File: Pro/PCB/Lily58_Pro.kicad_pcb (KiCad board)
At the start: 2 copper layers, 142.5 x 106.3 mm, 87 parts, among them J1 LED, J2 4PIN, J3 OLED, P1 i2c_pin, P2 i2c_pin, SW1 SW_PUSH, SW10 SW_PUSH, SW11 SW_PUSH, SW12 SW_PUSH, SW13 SW_PUSH, SW14 SW_PUSH, SW15 SW_PUSH, SW16 SW_PUSH, SW17 SW_PUSH, SW18 SW_PUSH, SW19 SW_PUSH, SW2 SW_PUSH, SW20 SW_PUSH, SW21 SW_PUSH, SW22 SW_PUSH, SW23 SW_PUSH, SW24 SW_PUSH, SW25 SW_PUSH, SW26 SW_PUSH, SW27 SW_PUSH, SW28 SW_PUSH, SW29 SW_PUSH, SW3 SW_PUSH, SW4 SW_PUSH, SW5 SW_PUSH, SW6 SW_PUSH, SW7 SW_PUSH, SW8 SW_PUSH, SW9 SW_PUSH, U1 ProMicro

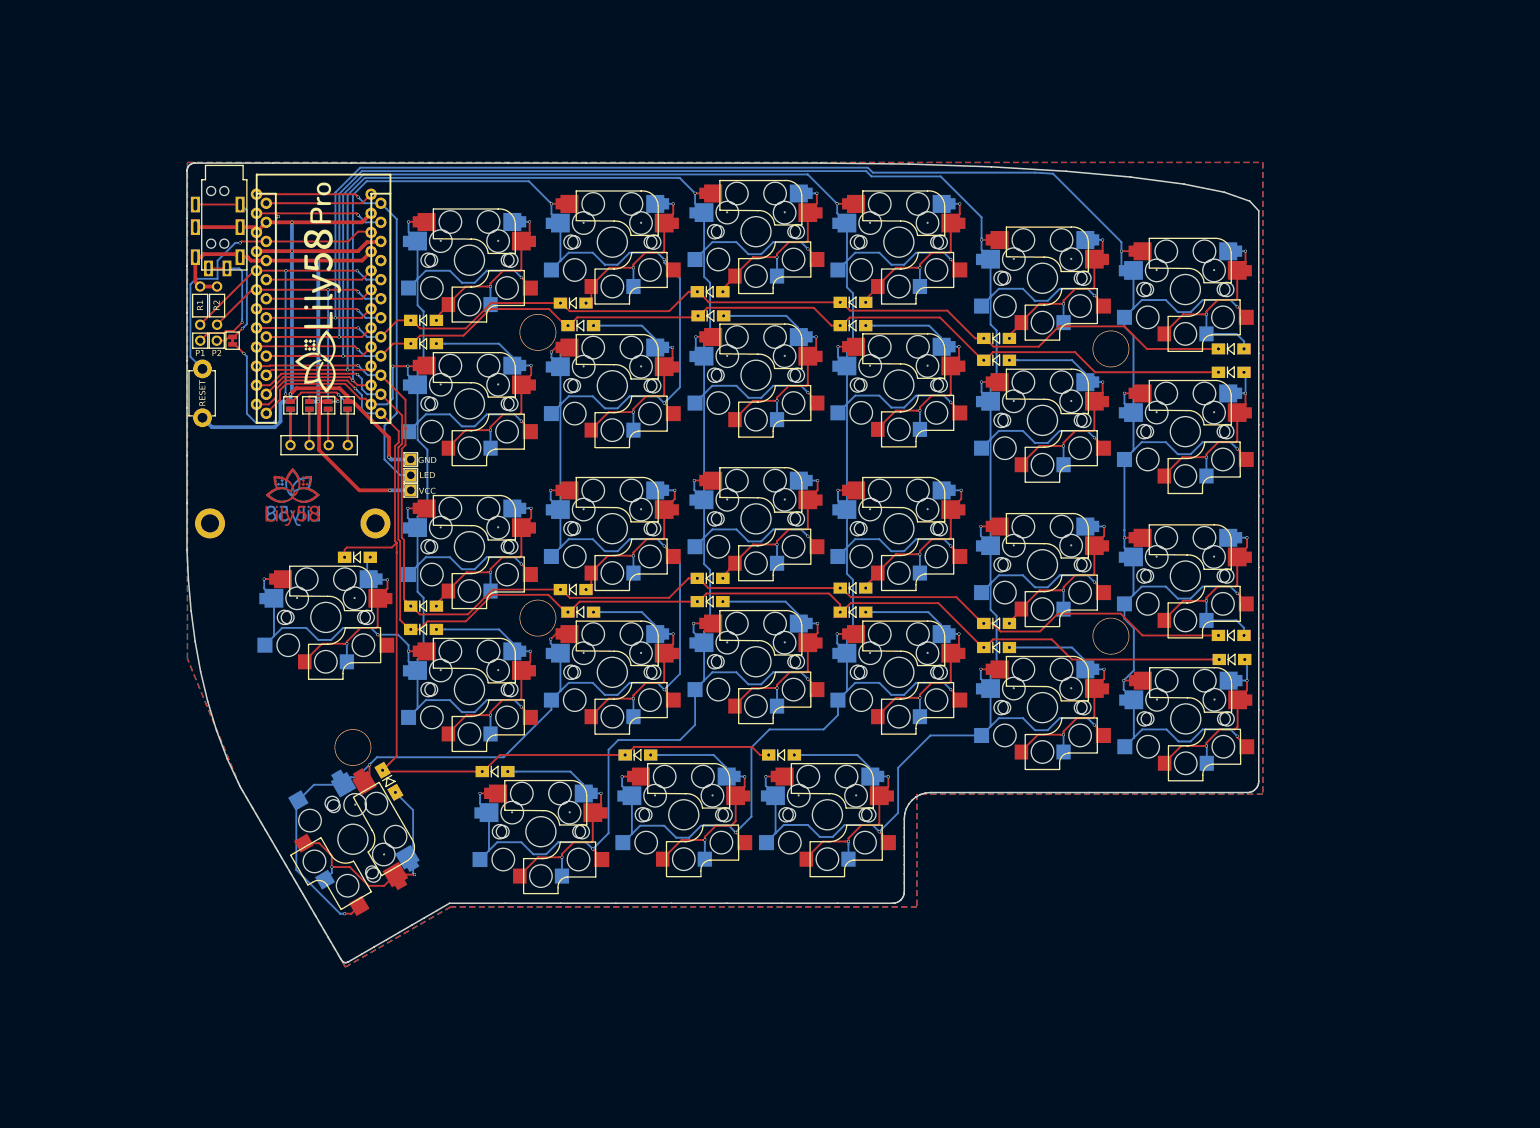
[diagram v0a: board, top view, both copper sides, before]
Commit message: Adjust thumb positions, add battery switch
Also powers/charges both sides
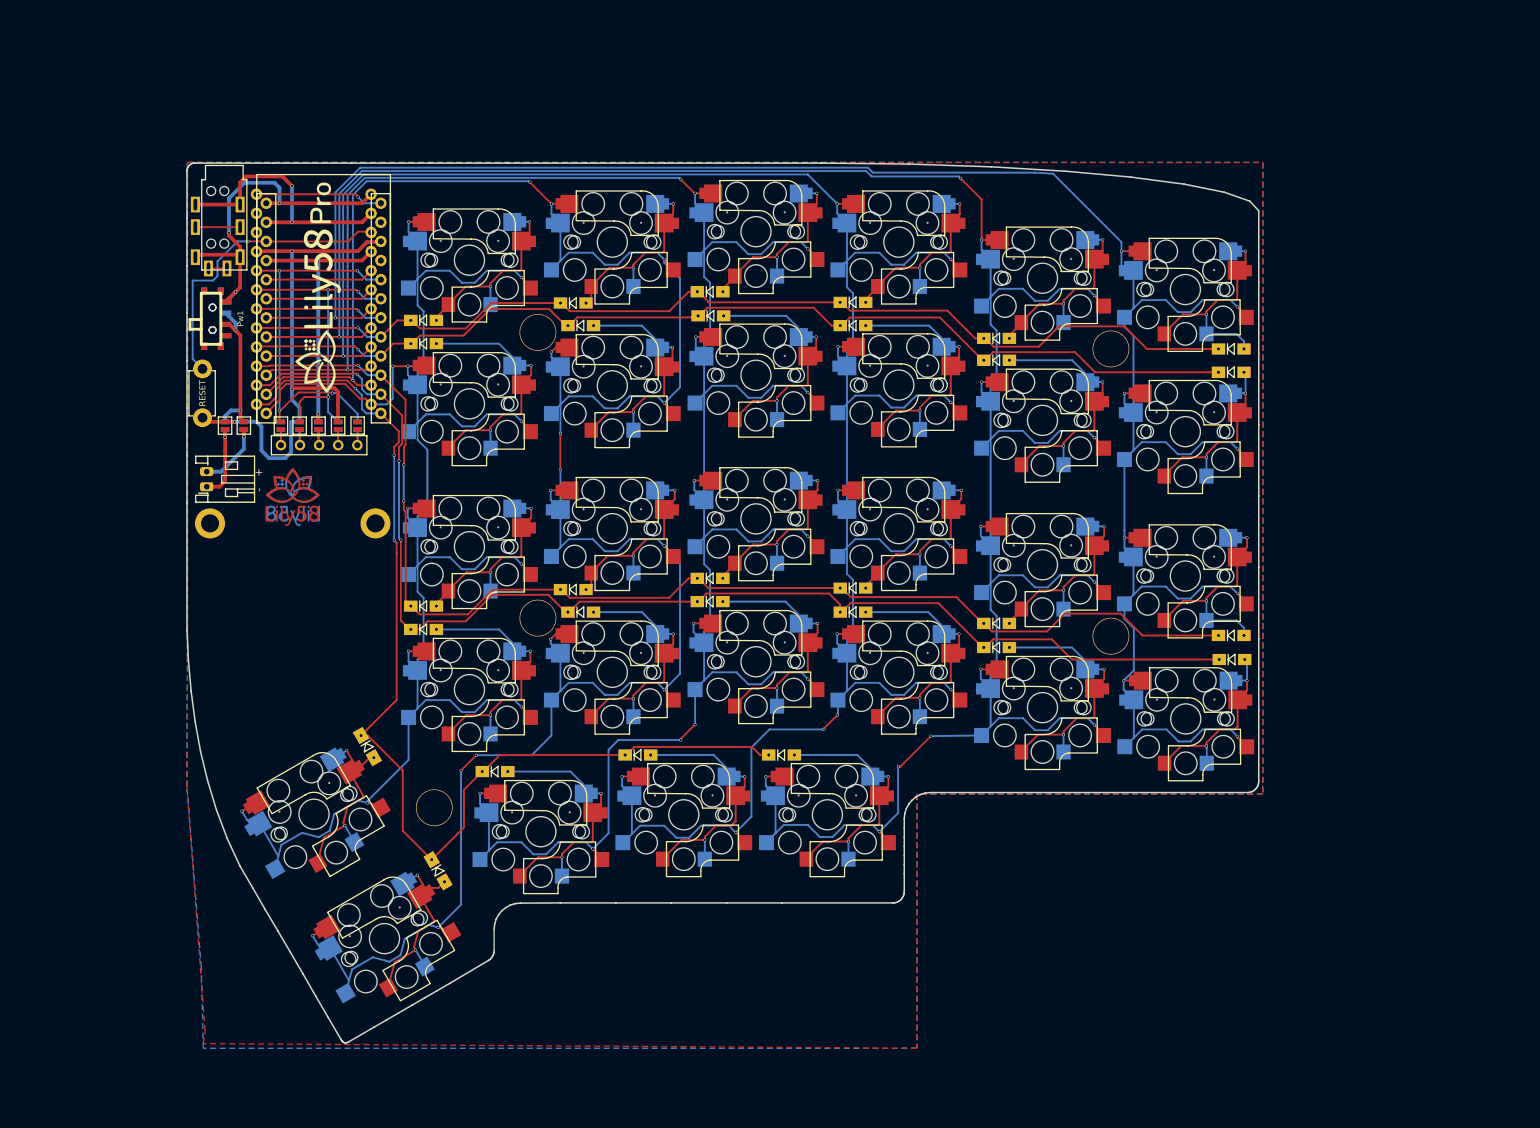
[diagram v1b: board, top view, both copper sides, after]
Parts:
- removed the J1 at (112.7, 81.1)
- removed P1, P2: i2c_pin, Lily58-footprint:1pin_conn
- removed R1, R2: R, Lily58-footprint:RESISTOR_mini
- removed W1: jumper, Lily58-footprint:jumper_data
- added BT1: Battery_Cell, Connector_JST:JST_PH_S2B-PH-K_1x02_P2.00mm_Horizontal, F.Cu at (85.6, 80.1)
- added JP1: Jumper_NO_Small, Lily58-footprint:Jumper, F.Cu at (105.6, 72.0)
- added JP11: Device:Jumper_NO_Small, Lily58-footprint:Jumper, F.Cu at (90.5, 72.0)
- added JP12: Device:Jumper_NO_Small, Lily58-footprint:Jumper, F.Cu at (88.0, 72.0)
- added JP13: Device:Jumper_NO_Small, Lily58-footprint:Jumper, B.Cu at (90.5, 72.0)
- added JP14: Device:Jumper_NO_Small, Lily58-footprint:Jumper, B.Cu at (88.0, 72.0)
- added JP6: JP6, Lily58-footprint:Jumper, B.Cu at (105.6, 72.0)
- added Pw1: SW_SPDT, open-project:SWITCH_ALPS_SSSS8, F.Cu at (84.8, 57.8)
- added Pw2: SW_SPDT, open-project:SWITCH_ALPS_SSSS8, B.Cu at (84.8, 57.8)
- JP10: renamed from JP8; value (none) -> Jumper_NO_Small
- JP2: renamed from JP1; value (none) -> Jumper_NO_Small
- JP3: renamed from JP2; value (none) -> Jumper_NO_Small
- JP4: renamed from JP3; value (none) -> Jumper_NO_Small
- JP5: renamed from JP4; value (none) -> Jumper_NO_Small
- JP7: renamed from JP5; value (none) -> Jumper_NO_Small
- JP8: renamed from JP6; value (none) -> Jumper_NO_Small
- JP9: renamed from JP7; value (none) -> Jumper_NO_Small
- SW1: footprint Lily58-footprint:CherryMX_KailhLowProfile_Hotswap_edge -> Lily58-footprint:MX_Choc_Hotswap
- SW10: renamed from SW26; footprint Lily58-footprint:CherryMX_KailhLowProfile_Hotswap_edge -> Lily58-footprint:MX_Choc_Hotswap
- SW11: renamed from SW3; footprint Lily58-footprint:CherryMX_KailhLowProfile_Hotswap_edge -> Lily58-footprint:MX_Choc_Hotswap
- SW12: renamed from SW9; footprint Lily58-footprint:CherryMX_KailhLowProfile_Hotswap_edge -> Lily58-footprint:MX_Choc_Hotswap
- SW13: renamed from SW15; footprint Lily58-footprint:CherryMX_KailhLowProfile_Hotswap_edge -> Lily58-footprint:MX_Choc_Hotswap
- SW14: renamed from SW21; footprint Lily58-footprint:CherryMX_KailhLowProfile_Hotswap_edge -> Lily58-footprint:MX_Choc_Hotswap
- SW15: renamed from SW27; footprint Lily58-footprint:CherryMX_KailhLowProfile_Hotswap_edge -> Lily58-footprint:MX_Choc_Hotswap
- SW16: renamed from SW4; footprint Lily58-footprint:CherryMX_KailhLowProfile_Hotswap_edge -> Lily58-footprint:MX_Choc_Hotswap
- SW17: renamed from SW10; footprint Lily58-footprint:CherryMX_KailhLowProfile_Hotswap_edge -> Lily58-footprint:MX_Choc_Hotswap
- SW18: renamed from SW16; footprint Lily58-footprint:CherryMX_KailhLowProfile_Hotswap_edge -> Lily58-footprint:MX_Choc_Hotswap
- SW19: renamed from SW22; footprint Lily58-footprint:CherryMX_KailhLowProfile_Hotswap_edge -> Lily58-footprint:MX_Choc_Hotswap
- SW2: renamed from SW7; footprint Lily58-footprint:CherryMX_KailhLowProfile_Hotswap_edge -> Lily58-footprint:MX_Choc_Hotswap
- SW20: renamed from SW28; footprint Lily58-footprint:CherryMX_KailhLowProfile_Hotswap_edge -> Lily58-footprint:MX_Choc_Hotswap
- SW21: renamed from SW5; footprint Lily58-footprint:CherryMX_KailhLowProfile_Hotswap_edge -> Lily58-footprint:MX_Choc_Hotswap
- SW22: renamed from SW11; footprint Lily58-footprint:CherryMX_KailhLowProfile_Hotswap_edge -> Lily58-footprint:MX_Choc_Hotswap
- SW23: renamed from SW17; footprint Lily58-footprint:CherryMX_KailhLowProfile_Hotswap_edge -> Lily58-footprint:MX_Choc_Hotswap
- SW24: renamed from SW23; footprint Lily58-footprint:CherryMX_KailhLowProfile_Hotswap_edge -> Lily58-footprint:MX_Choc_Hotswap
- SW25: renamed from SW29; footprint Lily58-footprint:CherryMX_KailhLowProfile_Hotswap_edge -> Lily58-footprint:MX_Choc_Hotswap
- SW26: renamed from SW6; footprint Lily58-footprint:CherryMX_KailhLowProfile_Hotswap_edge -> Lily58-footprint:MX_Choc_Hotswap
- SW27: renamed from SW12; footprint Lily58-footprint:CherryMX_KailhLowProfile_Hotswap_edge -> Lily58-footprint:MX_Choc_Hotswap
- SW28: renamed from SW18; footprint Lily58-footprint:CherryMX_KailhLowProfile_Hotswap_edge -> Lily58-footprint:MX_Choc_Hotswap
- SW29: renamed from SW24; footprint Lily58-footprint:CherryMX_KailhLowProfile_Hotswap_edge -> Lily58-footprint:MX_Choc_Hotswap
- SW3: renamed from SW13; footprint Lily58-footprint:CherryMX_KailhLowProfile_Hotswap_edge -> Lily58-footprint:MX_Choc_Hotswap
- SW4: renamed from SW19; footprint Lily58-footprint:CherryMX_KailhLowProfile_Hotswap_edge -> Lily58-footprint:MX_Choc_Hotswap
- SW5: renamed from SW25; footprint Lily58-footprint:CherryMX_KailhLowProfile_Hotswap_edge -> Lily58-footprint:MX_Choc_Hotswap
- SW6: renamed from SW2; footprint Lily58-footprint:CherryMX_KailhLowProfile_Hotswap_edge -> Lily58-footprint:MX_Choc_Hotswap
- SW7: renamed from SW8; footprint Lily58-footprint:CherryMX_KailhLowProfile_Hotswap_edge -> Lily58-footprint:MX_Choc_Hotswap
- SW8: renamed from SW14; footprint Lily58-footprint:CherryMX_KailhLowProfile_Hotswap_edge -> Lily58-footprint:MX_Choc_Hotswap
- SW9: renamed from SW20; footprint Lily58-footprint:CherryMX_KailhLowProfile_Hotswap_edge -> Lily58-footprint:MX_Choc_Hotswap
- U1: value ProMicro -> NiceNano
- moved SW5 26.2 mm to (99.8, 123.7), turned to 30 degrees
- moved D5 25.2 mm to (106.9, 114.7), turned to -60 degrees
- moved SW10 13.9 mm to (109.2, 140.2), turned to 30 degrees
- moved D10 13.6 mm to (116.3, 131.2)
- moved TH7 13.5 mm to (115.8, 122.8)
- moved JP4 2.99 mm to (97.9, 72.0)
- moved JP2 2.99 mm to (103.0, 72.0)
- moved JP3 2.99 mm to (100.4, 72.0)
- moved JP10 2.98 mm to (95.4, 72.0)
- moved JP5 2.98 mm to (95.4, 72.0)
- moved JP7 2.98 mm to (103.0, 72.0)
- moved JP8 2.98 mm to (100.4, 72.0)
- moved JP9 2.98 mm to (97.9, 72.0)
- moved J1 1.27 mm to (95.4, 74.6)
- renumbered D26 to D10, D3 to D11, D9 to D12, D15 to D13, D21 to D14, D27 to D15, D4 to D16, D10 to D17, D16 to D18, D22 to D19, D7 to D2, D28 to D20, D5 to D21, D11 to D22, D17 to D23, D23 to D24, D29 to D25, D6 to D26, D12 to D27, D18 to D28, D24 to D29, D13 to D3, D19 to D4, D25 to D5, D2 to D6, D8 to D7, D14 to D8, D20 to D9, J3 to J1
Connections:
- J2 pad 1: VCC -> POWER
- J2 pad 2: GND -> unconnected-(J2-Pad2)
- J2 pad 3: Net-(J2-Pad3) -> GND
- J2 pad 4: Net-(J2-Pad4) -> unconnected-(J2-Pad4)
- JP10 pad 2: GND -> CS
- JP7 pad 2: SDA -> SCL
- JP8 pad 2: SCL -> VCC
- JP9 pad 2: VCC -> GND
- U1 pad 1: LED -> CS
- U1 pad 19: Net-(U1-Pad19) -> unconnected-(U1-A2(PF5)-Pad19)
- U1 pad 2: DATA -> unconnected-(U1-RX(PD2)-Pad2)
- U1 pad 20: Net-(U1-Pad20) -> unconnected-(U1-A3(PF4)-Pad20)
- U1 pad 24: Net-(U1-Pad24) -> POWER
- U1 pad 7: Net-(U1-Pad7) -> unconnected-(U1-D4(PD4)-Pad7)
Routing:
- net DATA: track 59.7 -> 0.00 mm, vias 3 -> 0
- net LED: track 57.0 -> 0.00 mm, vias 1 -> 0
- net POWER: track 0.00 -> 46.7 mm, vias 0 -> 3
- net VCC: track 72.9 -> 36.9 mm, vias 3 -> 2
- net Net-(J2-Pad3): track 26.6 -> 0.00 mm, vias 1 -> 0
- net BAT_POS: track 0.00 -> 20.2 mm, vias 0 -> 2
- net Net-(J2-Pad4): track 17.9 -> 0.00 mm, vias 1 -> 0
- net unconnected-(U1-D4(PD4)-Pad7): track 0.00 -> 17.0 mm, vias 0 -> 1
- net Net-(U1-Pad7): track 17.0 -> 0.00 mm, vias 1 -> 0
- net CS: track 0.00 -> 17.0 mm, vias 0 -> 1
- net unconnected-(U1-A3(PF4)-Pad20): track 0.00 -> 14.4 mm
- net unconnected-(U1-A2(PF5)-Pad19): track 0.00 -> 14.4 mm
- net Net-(U1-Pad24): track 14.4 -> 0.00 mm
- net Net-(U1-Pad20): track 14.4 -> 0.00 mm
- net Net-(U1-Pad19): track 14.4 -> 0.00 mm
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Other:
- board size 142.5 x 106.3 mm -> 142.5 x 117 mm
- net class Default removed
- net class GND removed
- net class VCC removed

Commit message: v1
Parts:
- G*** (x2): footprint Lily58-footprint:lily58_logo_Pro -> Lily58-footprint:iri58_logo_Pro
- G*** (x2): footprint Lily58-footprint:lily58_logo_2 -> Lily58-footprint:iris58_logo_2
- moved TH7 25.4 mm to (94.8, 108.5)
- moved SW10 4.71 mm to (110.4, 135.7)
- moved SW5 4.60 mm to (100.9, 119.2)
- moved D10 4.30 mm to (117.1, 127.0)
- moved D5 4.24 mm to (107.7, 110.5)
- moved G*** 3.51 mm to (100.5, 81.5) (x2)
- moved G*** 1.62 mm to (100.4, 55.2)
- moved G*** 1.62 mm to (100.4, 55.3)
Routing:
- net row4: track 142.6 -> 137.3 mm, vias 3 -> 4
- net col4: track 321.7 -> 316.8 mm
- net col5: track 242.6 -> 238.3 mm, vias 11 -> 10
- net Net-(D5-A): track 27.7 -> 26.9 mm
- net Net-(D10-A): track 27.6 -> 26.9 mm
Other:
- board size 142.5 x 117 mm -> 142.5 x 112.3 mm

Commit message: v2
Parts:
- removed D10, D11, D12, D13, D14, D15, D16, D17, D18, D19, D2, D20, D21, D22, D23, D24, D25, D26, D27, D28, D29, D3, D4, D5, D6, D7, D8, D9: D, Lily58-footprint:Diode_SOD123
- removed the G*** at (100.4, 55.2)
- removed the G*** at (100.4, 55.3)
- removed the JP3 at (100.4, 72.0)
- removed the JP8 at (100.4, 72.0)
- removed U1: NiceNano, Lily58-footprint:ProMicro_rev2
- added ENC1: RotaryEncoder_Switch, Rotary_Encoder:RotaryEncoder_Alps_EC11E-Switch_Vertical_H20mm, F.Cu at (88.8, 93.3)
- added JP13: ~, Lily58-footprint:Jumper_arrow, F.Cu at (90.6, 87.5)
- added JP14: ~, Lily58-footprint:Jumper_arrow, F.Cu at (93.1, 87.5)
- added JP15: ~, Lily58-footprint:Jumper_arrow, B.Cu at (90.6, 87.5)
- added JP16: ~, Lily58-footprint:Jumper_arrow, B.Cu at (93.1, 87.5)
- added MCU1: NiceNano, Lily58-footprint:ProMicro_rev3, F.Cu at (100.7, 51.2)
- D1: value D -> Lily58-cache:D
- J1: footprint Lily58-footprint:OLED_4Pin -> Lily58-footprint:NiceView_5Pin
- J2: value 4PIN -> TRRS
- JP1, JP2: value Jumper_NO_Small -> ~; footprint Lily58-footprint:Jumper -> Lily58-footprint:Jumper_arrow
- JP10: renamed from JP12; value Device:Jumper_NO_Small -> ~; footprint Lily58-footprint:Jumper -> Lily58-footprint:Jumper_arrow
- JP11: renamed from JP13; value Device:Jumper_NO_Small -> ~; footprint Lily58-footprint:Jumper -> Lily58-footprint:Jumper_arrow
- JP12: renamed from JP14; value Device:Jumper_NO_Small -> ~; footprint Lily58-footprint:Jumper -> Lily58-footprint:Jumper_arrow
- JP3: renamed from JP4; value Jumper_NO_Small -> ~; footprint Lily58-footprint:Jumper -> Lily58-footprint:Jumper_arrow
- JP4: renamed from JP5; value Jumper_NO_Small -> ~; footprint Lily58-footprint:Jumper -> Lily58-footprint:Jumper_arrow
- JP5: renamed from JP6; value JP6 -> ~; footprint Lily58-footprint:Jumper -> Lily58-footprint:Jumper_arrow
- JP6: renamed from JP7; value Jumper_NO_Small -> ~; footprint Lily58-footprint:Jumper -> Lily58-footprint:Jumper_arrow
- JP7: renamed from JP9; value Jumper_NO_Small -> ~; footprint Lily58-footprint:Jumper -> Lily58-footprint:Jumper_arrow
- JP8: renamed from JP10; value Jumper_NO_Small -> ~; footprint Lily58-footprint:Jumper -> Lily58-footprint:Jumper_arrow
- JP9: renamed from JP11; value Device:Jumper_NO_Small -> ~; footprint Lily58-footprint:Jumper -> Lily58-footprint:Jumper_arrow
- SW1: footprint Lily58-footprint:MX_Choc_Hotswap -> Lily58-footprint:MX_Choc_Hotswap_bottom_diode
- SW10: renamed from SW17; footprint Lily58-footprint:MX_Choc_Hotswap -> Lily58-footprint:MX_Choc_Hotswap_bottom_diode
- SW11: renamed from SW22; footprint Lily58-footprint:MX_Choc_Hotswap -> Lily58-footprint:MX_Choc_Hotswap_bottom_diode
- SW12: renamed from SW27; footprint Lily58-footprint:MX_Choc_Hotswap -> Lily58-footprint:MX_Choc_Hotswap_bottom_diode
- SW13: renamed from SW3; footprint Lily58-footprint:MX_Choc_Hotswap -> Lily58-footprint:MX_Choc_Hotswap_bottom_diode
- SW14: renamed from SW8; footprint Lily58-footprint:MX_Choc_Hotswap -> Lily58-footprint:MX_Choc_Hotswap_bottom_diode
- SW15: renamed from SW13; footprint Lily58-footprint:MX_Choc_Hotswap -> Lily58-footprint:MX_Choc_Hotswap_bottom_diode
- SW16: renamed from SW18; footprint Lily58-footprint:MX_Choc_Hotswap -> Lily58-footprint:MX_Choc_Hotswap_bottom_diode
- SW17: renamed from SW23; footprint Lily58-footprint:MX_Choc_Hotswap -> Lily58-footprint:MX_Choc_Hotswap_bottom_diode
- SW18: renamed from SW28; footprint Lily58-footprint:MX_Choc_Hotswap -> Lily58-footprint:MX_Choc_Hotswap_bottom_diode
- SW19: renamed from SW4; footprint Lily58-footprint:MX_Choc_Hotswap -> Lily58-footprint:MX_Choc_Hotswap_bottom_diode
- SW2: renamed from SW6; footprint Lily58-footprint:MX_Choc_Hotswap -> Lily58-footprint:MX_Choc_Hotswap_bottom_diode
- SW20: renamed from SW9; footprint Lily58-footprint:MX_Choc_Hotswap -> Lily58-footprint:MX_Choc_Hotswap_bottom_diode
- SW21: renamed from SW14; footprint Lily58-footprint:MX_Choc_Hotswap -> Lily58-footprint:MX_Choc_Hotswap_bottom_diode
- SW22: renamed from SW19; footprint Lily58-footprint:MX_Choc_Hotswap -> Lily58-footprint:MX_Choc_Hotswap_bottom_diode
- SW23: renamed from SW24; footprint Lily58-footprint:MX_Choc_Hotswap -> Lily58-footprint:MX_Choc_Hotswap_bottom_diode
- SW24: renamed from SW29; footprint Lily58-footprint:MX_Choc_Hotswap -> Lily58-footprint:MX_Choc_Hotswap_bottom_diode
- SW25: renamed from SW5; footprint Lily58-footprint:MX_Choc_Hotswap -> Lily58-footprint:MX_Choc_Hotswap_right_diode
- SW26: renamed from SW10; footprint Lily58-footprint:MX_Choc_Hotswap -> Lily58-footprint:MX_Choc_Hotswap_right_diode
- SW27: renamed from SW15; footprint Lily58-footprint:MX_Choc_Hotswap -> Lily58-footprint:MX_Choc_Hotswap_top_diode
- SW28: renamed from SW20; footprint Lily58-footprint:MX_Choc_Hotswap -> Lily58-footprint:MX_Choc_Hotswap_top_diode
- SW29: renamed from SW25; footprint Lily58-footprint:MX_Choc_Hotswap -> Lily58-footprint:MX_Choc_Hotswap_top_diode
- SW3: renamed from SW11; footprint Lily58-footprint:MX_Choc_Hotswap -> Lily58-footprint:MX_Choc_Hotswap_bottom_diode
- SW4: renamed from SW16; footprint Lily58-footprint:MX_Choc_Hotswap -> Lily58-footprint:MX_Choc_Hotswap_bottom_diode
- SW5: renamed from SW21; footprint Lily58-footprint:MX_Choc_Hotswap -> Lily58-footprint:MX_Choc_Hotswap_bottom_diode
- SW6: renamed from SW26; footprint Lily58-footprint:MX_Choc_Hotswap -> Lily58-footprint:MX_Choc_Hotswap_bottom_diode
- SW7: renamed from SW2; footprint Lily58-footprint:MX_Choc_Hotswap -> Lily58-footprint:MX_Choc_Hotswap_bottom_diode
- SW8: renamed from SW7; footprint Lily58-footprint:MX_Choc_Hotswap -> Lily58-footprint:MX_Choc_Hotswap_bottom_diode
- SW9: renamed from SW12; footprint Lily58-footprint:MX_Choc_Hotswap -> Lily58-footprint:MX_Choc_Hotswap_bottom_diode
- TH3, TH4, TH5, TH6, TH7: footprint Lily58-footprint:HOLE_M2_TH -> Lily58-footprint:HOLE_M2_Standoff
- moved D1 39.3 mm to (106.4, 96.5), turned to -90 degrees
- moved TH7 0.33 mm to (94.6, 108.2)
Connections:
- net POWER renamed RAW
- D1 pad 1: row0 -> row4
- J1 pad 3: Net-(J1-P3) -> VCC
- SW1 pad 2: Net-(D1-A) -> Net-(SW1-Pad2)
- SW25 pad 1: col5 -> col4
- SW26 pad 1: col4 -> col3
- SW27 pad 1: col3 -> col2
- SW28 pad 1: col2 -> col1
- SW29 pad 1: col1 -> col0
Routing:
- net col3: track 317.0 -> 82.1 mm, vias 14 -> 1
- net col4: track 316.8 -> 85.6 mm, vias 16 -> 1
- net col5: track 238.3 -> 50.6 mm, vias 10 -> 1
- net col2: track 333.1 -> 162.3 mm, vias 13 -> 1
- net col1: track 350.6 -> 180.9 mm, vias 14 -> 1
- net col0: track 303.4 -> 192.6 mm, vias 9 -> 1
- net CS: track 17.0 -> 65.0 mm, vias 1 -> 4
- net encA: track 0.00 -> 44.8 mm, vias 0 -> 2
- net encB: track 0.00 -> 40.3 mm, vias 0 -> 1
- net Net-(SW7-Pad2): track 37.2 -> 0.00 mm, vias 2 -> 0
- net Net-(SW19-Pad2): track 37.1 -> 0.00 mm, vias 2 -> 0
- net Net-(SW28-Pad2): track 37.0 -> 0.00 mm, vias 2 -> 0
- net Net-(SW21-Pad2): track 37.0 -> 0.00 mm, vias 2 -> 0
- net Net-(SW23-Pad2): track 36.9 -> 0.00 mm, vias 2 -> 0
- net Net-(SW29-Pad2): track 36.8 -> 0.00 mm, vias 2 -> 0
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- added copper zone on B.Cu, net (none)
- added copper zone on F.Cu, net (none)
- removed copper zone on B.Cu, net GND
- removed copper zone on F.Cu, net GND
